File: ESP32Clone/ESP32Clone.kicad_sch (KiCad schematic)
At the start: 55 parts, among them J1 Connector, USB-TYPE-C-16P, J2 Conn_01x08_Pin, J3 Conn_01x08_Pin, U1 TPS54331DR, U2 ESP32-C3FH4, U3 AHT20, U4 BH1750FVI-TR, U5 24LC1025-I_SM, X1 40MHz, 15pF

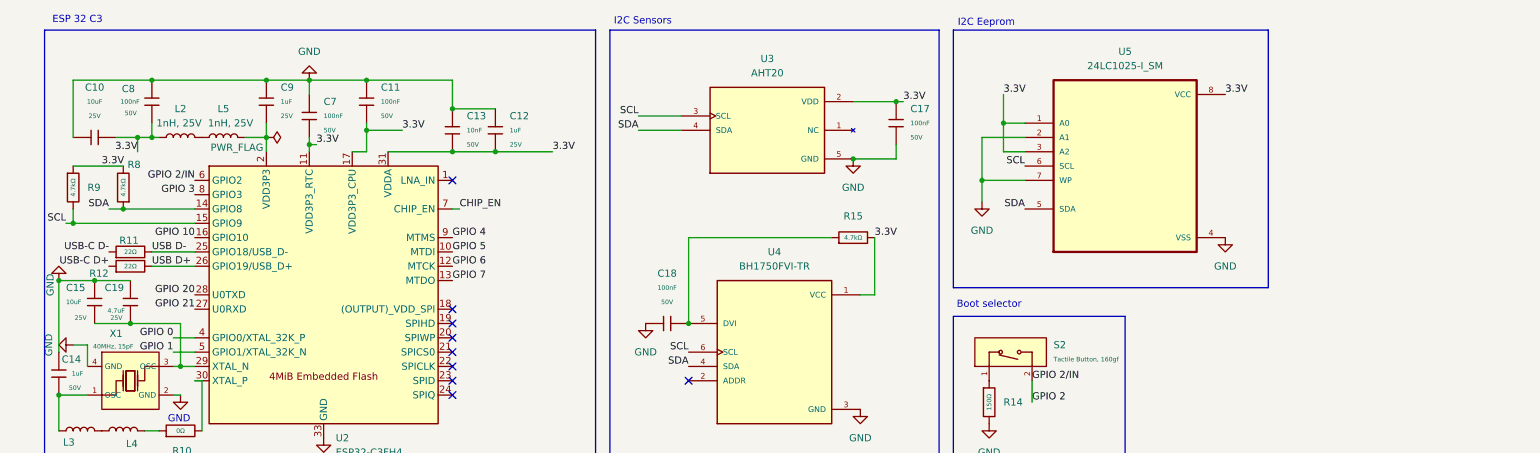
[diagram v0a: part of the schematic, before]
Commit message: Added mounting holes and fixed erc warnings
ERC warning remaining:
Pin no connection type is connected, its connected to a no connect flag somehow thats a warning.
Both Gpio 2 GPIO 2/IN are connected to the same item. this is correct it has to do with the boot select
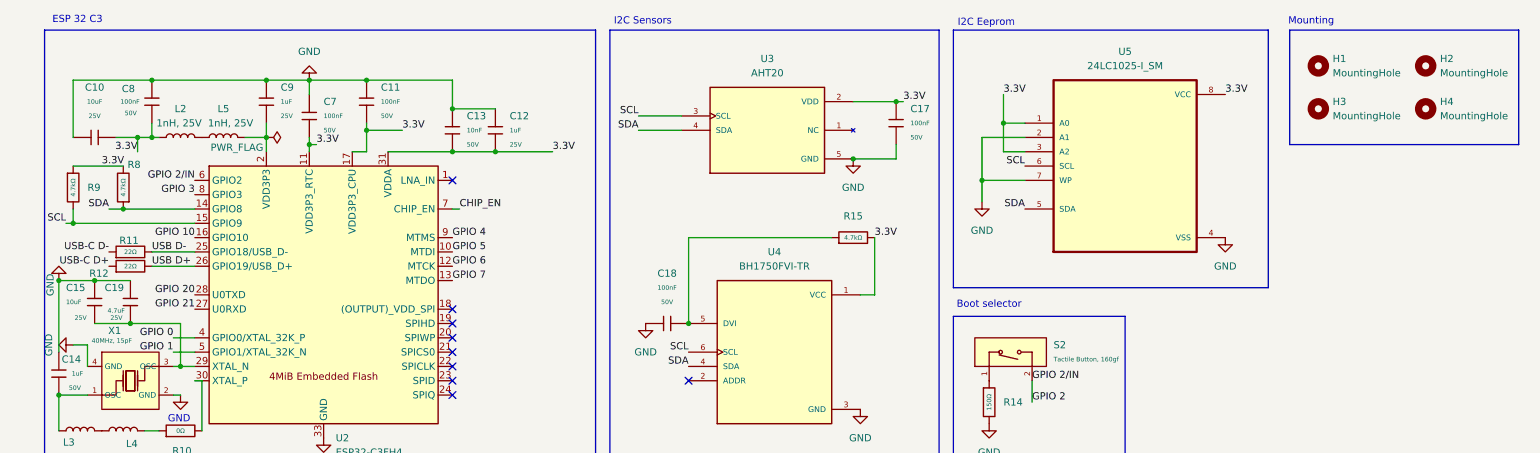
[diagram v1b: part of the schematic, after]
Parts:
- added H1, H2, H3, H4: MountingHole, MountingHole:MountingHole_2.1mm, symbol Mechanical:MountingHole
- L1: symbol INDUCTER-JLC-Extended:SRP4020TA-4R7M -> SRP4020TA-4R7M:SRP4020TA-4R7M
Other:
- note added: "Mounting"

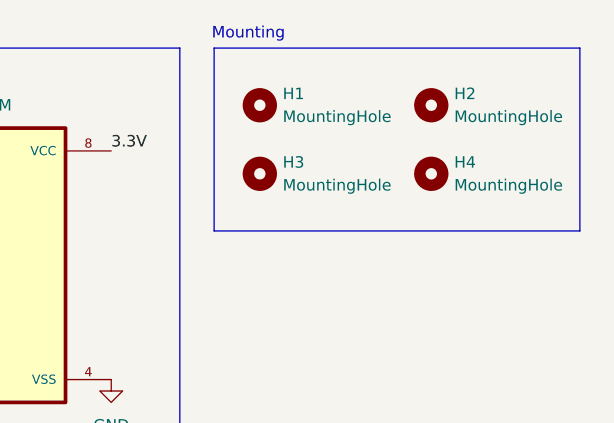
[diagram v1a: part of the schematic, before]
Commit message: Fixed DRC
DRC remianing:
3x Koala figure silkscreen clipped by something,
the koala is giant and doesnt give importent information so its fine
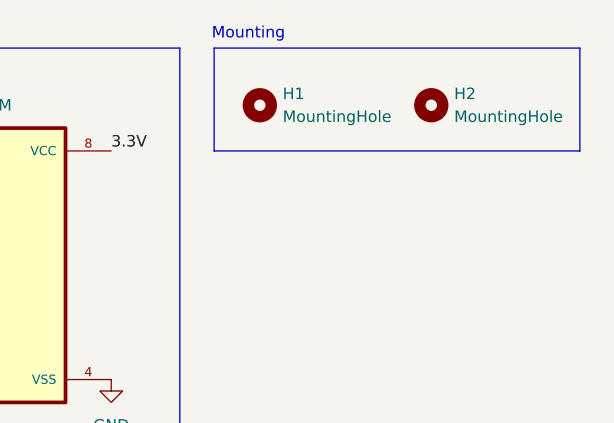
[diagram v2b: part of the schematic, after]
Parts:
- removed H3, H4: MountingHole, MountingHole:MountingHole_2.1mm, symbol Mechanical:MountingHole
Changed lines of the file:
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@@
 	(rectangle
 		(start 234.95 15.24)
-		(end 275.59 35.56)
+		(end 275.59 26.67)
 		(stroke
 			(width 0)
@@
 	)
 	(symbol
-		(lib_id "Mechanical:MountingHole")
-		(at 259.08 29.21 0)
-		(unit 1)
-		(exclude_from_sim no)
-		(in_bom no)
-		(on_board yes)
-		(dnp no)
-		(fields_autoplaced yes)
-		(property "Reference" "H4"
-			(at 261.62 27.9399 0)
-			(effects
-				(font
-					(size 1.27 1.27)
-				)
-				(justify left)
-			)
-		)
-		(property "Value" "MountingHole"
-			(at 261.62 30.4799 0)
-			(effects
-				(font
-					(size 1.27 1.27)
-				)
-				(justify left)
-			)
-		)
-		(property "Footprint" "MountingHole:MountingHole_2.1mm"
-			(at 259.08 29.21 0)
-			(effects
-				(font
-					(size 1.27 1.27)
-				)
-				(hide yes)
-			)
-		)
-		(property "Datasheet" "~"
-			(at 259.08 29.21 0)
-			(effects
-				(font
-					(size 1.27 1.27)
-				)
-				(hide yes)
-			)
-		)
-		(property "Description" "Mounting Hole without connection"
-			(at 259.08 29.21 0)
-			(effects
-				(font
-					(size 1.27 1.27)
-				)
-				(hide yes)
-			)
-		)
-		(instances
-			(project ""
-				(path "/dd1e1a69-fb6d-4ec9-9346-c5821cbac777"
-					(reference "H4")
-					(unit 1)
-				)
-			)
-		)
-	)
-	(symbol
 		(lib_id "24LC1025-I_SM:24LC1025-I_SM")
 		(at 205.74 39.37 0)
@@
 					(unit 1)
 				)
-			)
-		)
-	)
-	(symbol
-		(lib_id "Mechanical:MountingHole")
-		(at 240.03 29.21 0)
-		(unit 1)
-		(exclude_from_sim no)
-		(in_bom no)
-		(on_board yes)
-		(dnp no)
-		(fields_autoplaced yes)
-		(property "Reference" "H3"
-			(at 242.57 27.9399 0)
-			(effects
-				(font
-					(size 1.27 1.27)
-				)
-				(justify left)
-			)
-		)
-		(property "Value" "MountingHole"
-			(at 242.57 30.4799 0)
-			(effects
-				(font
-					(size 1.27 1.27)
-				)
-				(justify left)
-			)
-		)
-		(property "Footprint" "MountingHole:MountingHole_2.1mm"
-			(at 240.03 29.21 0)
-			(effects
-				(font
-					(size 1.27 1.27)
-				)
-				(hide yes)
-			)
-		)
-		(property "Datasheet" "~"
-			(at 240.03 29.21 0)
-			(effects
-				(font
-					(size 1.27 1.27)
-				)
-				(hide yes)
-			)
-		)
-		(property "Description" "Mounting Hole without connection"
-			(at 240.03 29.21 0)
-			(effects
-				(font
-					(size 1.27 1.27)
-				)
-				(hide yes)
-			)
-		)
-		(instances
-			(project ""
-				(path "/dd1e1a69-fb6d-4ec9-9346-c5821cbac777"
-					(reference "H3")
-					(unit 1)
-				)

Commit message: removed a few islands and generated bom
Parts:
- J1: Part (none) -> USB-TYPE-C-019
- J2, J3: Part (none) -> CS-1109-1X8(L11.5)PA6T
- L1: Part (none) -> SRP4020TA-4R7M
- L2, L5: Part (none) -> VHF160808H1N0ST
- U2: Part (none) -> ESP32-C3FH4
- U3: Part (none) -> AHT20
- U4: Part (none) -> BH1750FVI-TR
- U5: Part (none) -> 24LC1025-I/SM
- X1: Part (none) -> X322540MPB4SI
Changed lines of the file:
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@@
 			)
 		)
+		(property "Part" "CS-1109-1X8(L11.5)PA6T"
+			(at 22.86 124.46 0)
+			(effects
+				(font
+					(size 1.27 1.27)
+				)
+				(hide yes)
+			)
+		)
 		(pin "5"
 		)
@@
 			)
 		)
+		(property "Part" "BH1750FVI-TR"
+			(at 143.51 72.39 0)
+			(effects
+				(font
+					(size 1.27 1.27)
+				)
+				(hide yes)
+			)
+		)
 		(pin "1"
 		)
@@
 			)
 		)
+		(property "Part" "VHF160808H1N0ST"
+			(at 45.72 34.29 90)
+			(effects
+				(font
+					(size 1.27 1.27)
+				)
+				(hide yes)
+			)
+		)
 		(pin "1"
 		)
@@
 			)
 		)
+		(property "Part" "24LC1025-I/SM"
+			(at 205.74 39.37 0)
+			(effects
+				(font
+					(size 1.27 1.27)
+				)
+				(hide yes)
+			)
+		)
 		(pin "4"
 		)
@@
 			)
 		)
+		(property "Part" "VHF160808H1N0ST"
+			(at 38.1 34.29 90)
+			(effects
+				(font
+					(size 1.27 1.27)
+				)
+				(hide yes)
+			)
+		)
 		(pin "1"
 		)
@@
 			)
 		)
+		(property "Part" "SRP4020TA-4R7M"
+			(at 111.76 162.56 0)
+			(effects
+				(font
+					(size 1.27 1.27)
+				)
+				(hide yes)
+			)
+		)
 		(pin "1"
 		)
@@
 			)
 		)
+		(property "Part" "USB-TYPE-C-019"
+			(at 24.13 165.1 0)
+			(effects
+				(font
+					(size 1.27 1.27)
+				)
+				(hide yes)
+			)
+		)
 		(pin "B9A4"
 		)
@@
 			)
 		)
+		(property "Part" "X322540MPB4SI"
+			(at 29.21 77.47 0)
+			(effects
+				(font
+					(size 1.27 1.27)
+				)
+				(hide yes)
+			)
+		)
 		(pin "2"
 		)
@@
 			)
 		)
+		(property "Part" "CS-1109-1X8(L11.5)PA6T"
+			(at 60.96 124.46 0)
+			(effects
+				(font
+					(size 1.27 1.27)
+				)
+				(hide yes)
+			)
+		)
 		(pin "3"
 		)
@@
 			)
 		)
+		(property "Part" "ESP32-C3FH4"
+			(at 63.5 62.23 0)
+			(effects
+				(font
+					(size 1.27 1.27)
+				)
+				(hide yes)
+			)
+		)
 		(pin "21"
 		)
@@
 			(at 142.24 33.02 0)
 			(effects
+				(font
+					(size 1.27 1.27)
+				)
+				(hide yes)
+			)
+		)
+		(property "Part" "AHT20"
+			(at 142.24 33.02 0)
+			(effects
